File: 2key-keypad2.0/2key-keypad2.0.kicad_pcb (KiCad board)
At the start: 2 copper layers, 39.7 x 43.7 mm, 21 parts, among them SW1 SW_Push, U2 ATmega32U2-AU, Y1 16MHz

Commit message: Updated Schem
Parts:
- moved C2 9.05 mm to (141.4, 89.7), turned to 135 degrees
- moved C3 9.00 mm to (135.0, 96.1), turned to -45 degrees
- moved R4 0.47 mm to (125.9, 93.3)
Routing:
- net +5V: track 0.00 -> 90.1 mm, vias 0 -> 4
- net GND: track 6.34 -> 42.8 mm, vias 0 -> 1
- net Net-(D1-DOUT): track 0.00 -> 31.4 mm, vias 0 -> 2
- net COL0: track 0.00 -> 22.3 mm
- net D-: track 0.00 -> 22.2 mm, vias 0 -> 2
- net Net-(U2-PC1/~{RESET}): track 0.00 -> 20.0 mm, vias 0 -> 2
- net D+: track 0.00 -> 19.9 mm
- net COL1: track 0.00 -> 19.8 mm, vias 0 -> 2
- net VCC: track 0.00 -> 18.9 mm
- net XTAL1: track 0.00 -> 10.8 mm
- net LED: track 0.00 -> 7.85 mm
- net Net-(U2-UCAP): track 0.00 -> 7.63 mm
- net XTAL2: track 0.00 -> 7.24 mm
- net Net-(U2-D+): track 0.00 -> 6.96 mm
- net Net-(U2-D-): track 0.00 -> 5.49 mm
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- added copper zone on B.Cu, net GND
- added copper zone on F.Cu, net GND

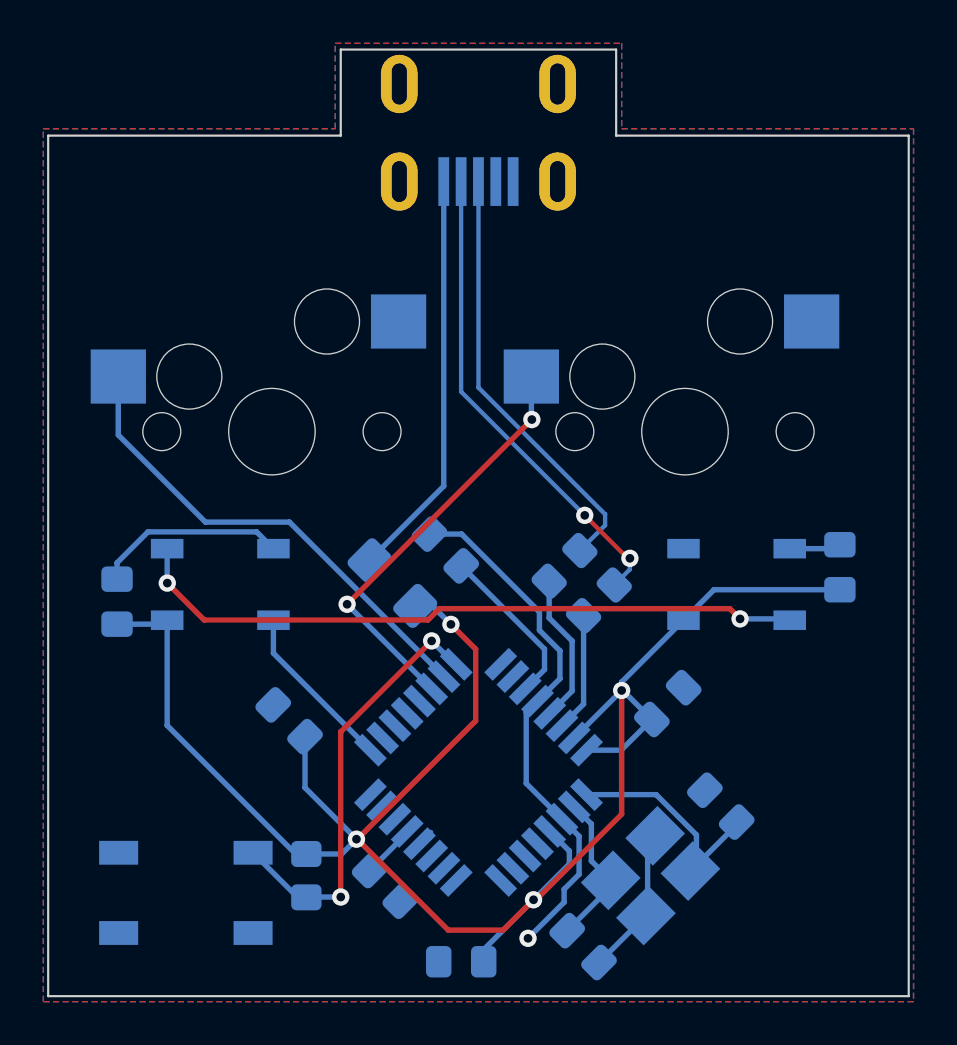
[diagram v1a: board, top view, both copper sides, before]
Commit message: Removed VIAs and equalized data traces
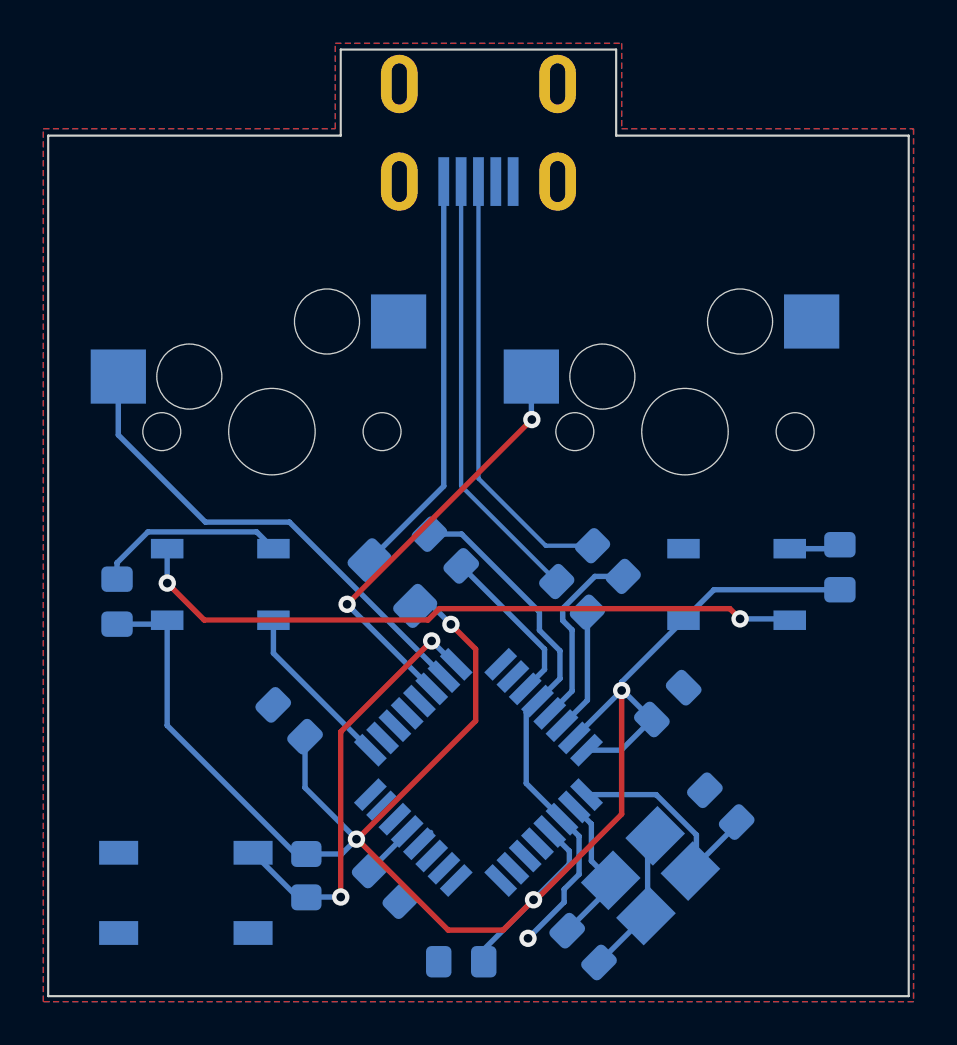
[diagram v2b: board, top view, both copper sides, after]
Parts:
- moved R1 2.01 mm to (136.1, 78.4), turned to -45 degrees
- moved R2 1.25 mm to (134.5, 80.0), turned to -45 degrees
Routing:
- net D-: track 22.2 -> 20.3 mm, vias 2 -> 0
- net Net-(U2-D+): track 6.96 -> 8.85 mm
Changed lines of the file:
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@@
   )
   (footprint "Resistor_SMD:R_0805_2012Metric_Pad1.20x1.40mm_HandSolder" (layer "B.Cu")
-    (at 135.73125 80.16875 -135)
+    (at 134.493 80.01 -45)
     (descr "Resistor SMD 0805 (2012 Metric), square (rectangular) end terminal, IPC_7351 nominal with elongated pad for handsoldering. (Body size source: IPC-SM-782 page 72, https://www.pcb-3d.com/wordpress/wp-content/uploads/ipc-sm-782a_amendment_1_and_2.pdf), generated with kicad-footprint-generator")
     (tags "resistor handsolder")
@@
     (property "ki_keywords" "R resistor")
     (attr smd)
-    (fp_text reference "R2" (at -2.918583 0.538815 45) (layer "B.SilkS")
-        (effects (font (size 1 1) (thickness 0.15)) (justify mirror))
-    )
-    (fp_text value "22" (at 0 -1.65 45) (layer "B.Fab")
-        (effects (font (size 1 1) (thickness 0.15)) (justify mirror))
-    )
-    (fp_text user "${REFERENCE}" (at 0 0 45) (layer "B.Fab")
+    (fp_text reference "R2" (at -2.918583 0.538815 135) (layer "B.SilkS")
+        (effects (font (size 1 1) (thickness 0.15)) (justify mirror))
+    )
+    (fp_text value "22" (at 0 -1.65 135) (layer "B.Fab")
+        (effects (font (size 1 1) (thickness 0.15)) (justify mirror))
+    )
+    (fp_text user "${REFERENCE}" (at 0 0 135) (layer "B.Fab")
         (effects (font (size 0.5 0.5) (thickness 0.08)) (justify mirror))
     )
@@
     (fp_line (start 1 0.625) (end 1 -0.625)
       (stroke (width 0.1) (type solid)) (layer "B.Fab"))
-    (pad "1" smd roundrect (at -1 0 225) (size 1.2 1.4) (layers "B.Cu" "B.Paste" "B.Mask") (roundrect_rratio 0.2083333333)
+    (pad "1" smd roundrect (at -1 0 315) (size 1.2 1.4) (layers "B.Cu" "B.Paste" "B.Mask") (roundrect_rratio 0.2083333333)
       (net 14 "D-") (pintype "passive"))
-    (pad "2" smd roundrect (at 1 0 225) (size 1.2 1.4) (layers "B.Cu" "B.Paste" "B.Mask") (roundrect_rratio 0.2083333333)
+    (pad "2" smd roundrect (at 1 0 315) (size 1.2 1.4) (layers "B.Cu" "B.Paste" "B.Mask") (roundrect_rratio 0.2083333333)
       (net 15 "Net-(U2-D-)") (pintype "passive"))
     (model "${KICAD6_3DMODEL_DIR}/Resistor_SMD.3dshapes/R_0805_2012Metric.wrl"
@@
   )
   (footprint "Resistor_SMD:R_0805_2012Metric_Pad1.20x1.40mm_HandSolder" (layer "B.Cu")
-    (at 134.14375 78.58125 -135)
+    (at 136.144 78.359 -45)
     (descr "Resistor SMD 0805 (2012 Metric), square (rectangular) end terminal, IPC_7351 nominal with elongated pad for handsoldering. (Body size source: IPC-SM-782 page 72, https://www.pcb-3d.com/wordpress/wp-content/uploads/ipc-sm-782a_amendment_1_and_2.pdf), generated with kicad-footprint-generator")
     (tags "resistor handsolder")
@@
     (property "ki_keywords" "R resistor")
     (attr smd)
-    (fp_text reference "R1" (at -2.828781 0 45) (layer "B.SilkS")
-        (effects (font (size 1 1) (thickness 0.15)) (justify mirror))
-    )
-    (fp_text value "22" (at 0 -1.65 45) (layer "B.Fab")
-        (effects (font (size 1 1) (thickness 0.15)) (justify mirror))
-    )
-    (fp_text user "${REFERENCE}" (at 0 0 45) (layer "B.Fab")
+    (fp_text reference "R1" (at -2.828781 0 135) (layer "B.SilkS")
+        (effects (font (size 1 1) (thickness 0.15)) (justify mirror))
+    )
+    (fp_text value "22" (at 0 -1.65 135) (layer "B.Fab")
+        (effects (font (size 1 1) (thickness 0.15)) (justify mirror))
+    )
+    (fp_text user "${REFERENCE}" (at 0 0 135) (layer "B.Fab")
         (effects (font (size 0.5 0.5) (thickness 0.08)) (justify mirror))
     )
@@
     (fp_line (start 1 0.625) (end 1 -0.625)
       (stroke (width 0.1) (type solid)) (layer "B.Fab"))
-    (pad "1" smd roundrect (at -1 0 225) (size 1.2 1.4) (layers "B.Cu" "B.Paste" "B.Mask") (roundrect_rratio 0.2083333333)
+    (pad "1" smd roundrect (at -1 0 315) (size 1.2 1.4) (layers "B.Cu" "B.Paste" "B.Mask") (roundrect_rratio 0.2083333333)
       (net 12 "D+") (pintype "passive"))
-    (pad "2" smd roundrect (at 1 0 225) (size 1.2 1.4) (layers "B.Cu" "B.Paste" "B.Mask") (roundrect_rratio 0.2083333333)
+    (pad "2" smd roundrect (at 1 0 315) (size 1.2 1.4) (layers "B.Cu" "B.Paste" "B.Mask") (roundrect_rratio 0.2083333333)
       (net 13 "Net-(U2-D+)") (pintype "passive"))
     (model "${KICAD6_3DMODEL_DIR}/Resistor_SMD.3dshapes/R_0805_2012Metric.wrl"
@@
   (segment (start 132.615 69.85) (end 132.615 71.81002) (width 0.25) (layer "B.Cu") (net 11))
   (segment (start 124.117903 80.352097) (end 123.952 80.186194) (width 0.25) (layer "B.Cu") (net 11))
-  (segment (start 130.175 70.359264) (end 136.015736 76.2) (width 0.2) (layer "B.Cu") (net 12))
-  (segment (start 136.017 76.2) (end 136.017 76.708) (width 0.2) (layer "B.Cu") (net 12))
-  (segment (start 136.017 76.708) (end 134.850857 77.874143) (width 0.2) (layer "B.Cu") (net 12))
-  (segment (start 136.015736 76.2) (end 136.017 76.2) (width 0.2) (layer "B.Cu") (net 12))
-  (segment (start 130.175 60.85625) (end 130.175 70.359264) (width 0.2) (layer "B.Cu") (net 12))
-  (segment (start 134.493 82.042) (end 134.493 84.353936) (width 0.25) (layer "B.Cu") (net 13))
+  (segment (start 130.175 60.85625) (end 130.175 74.549) (width 0.2) (layer "B.Cu") (net 12))
+  (segment (start 133.277893 77.651893) (end 135.436893 77.651893) (width 0.2) (layer "B.Cu") (net 12))
+  (segment (start 130.175 74.549) (end 133.277893 77.651893) (width 0.2) (layer "B.Cu") (net 12))
+  (segment (start 134.493 81.534) (end 134.493 84.353936) (width 0.25) (layer "B.Cu") (net 13))
   (segment (start 134.493 84.353936) (end 133.463047 85.383889) (width 0.25) (layer "B.Cu") (net 13))
-  (segment (start 133.436643 79.288357) (end 133.436643 80.985643) (width 0.25) (layer "B.Cu") (net 13))
-  (segment (start 133.436643 80.985643) (end 134.493 82.042) (width 0.25) (layer "B.Cu") (net 13))
-  (segment (start 137.058492 78.232) (end 137.16 78.232) (width 0.2) (layer "F.Cu") (net 14))
-  (segment (start 135.077246 76.250754) (end 137.058492 78.232) (width 0.2) (layer "F.Cu") (net 14))
-  (via (at 137.16 78.232) (size 0.8) (drill 0.4) (layers "F.Cu" "B.Cu") (net 14))
-  (via (at 135.077246 76.250754) (size 0.8) (drill 0.4) (layers "F.Cu" "B.Cu") (net 14))
-  (segment (start 129.375 70.548508) (end 135.077246 76.250754) (width 0.2) (layer "B.Cu") (net 14))
-  (segment (start 137.16 78.74) (end 136.438357 79.461643) (width 0.2) (layer "B.Cu") (net 14))
-  (segment (start 137.16 78.232) (end 137.16 78.74) (width 0.2) (layer "B.Cu") (net 14))
-  (segment (start 129.375 60.85625) (end 129.375 70.548508) (width 0.2) (layer "B.Cu") (net 14))
-  (segment (start 135.024143 84.954163) (end 134.028732 85.949574) (width 0.25) (layer "B.Cu") (net 15))
-  (segment (start 135.024143 80.875857) (end 135.024143 84.954163) (width 0.25) (layer "B.Cu") (net 15))
+  (segment (start 134.059421 81.100421) (end 134.493 81.534) (width 0.25) (layer "B.Cu") (net 13))
+  (segment (start 136.851107 79.066107) (end 135.542959 79.066107) (width 0.25) (layer "B.Cu") (net 13))
+  (segment (start 135.542959 79.066107) (end 134.059421 80.549645) (width 0.25) (layer "B.Cu") (net 13))
+  (segment (start 134.059421 80.549645) (end 134.059421 81.100421) (width 0.25) (layer "B.Cu") (net 13))
+  (segment (start 129.375 74.892) (end 133.785893 79.302893) (width 0.2) (layer "B.Cu") (net 14))
+  (segment (start 129.375 60.85625) (end 129.375 74.892) (width 0.2) (layer "B.Cu") (net 14))
+  (segment (start 135.200107 84.778199) (end 134.028732 85.949574) (width 0.25) (layer "B.Cu") (net 15))
+  (segment (start 135.200107 80.717107) (end 135.200107 84.778199) (width 0.25) (layer "B.Cu") (net 15))
   (segment (start 128.016 82.042) (end 123.825 86.233) (width 0.25) (layer "F.Cu") (net 16))
   (segment (start 123.825 86.233) (end 123.825 93.853) (width 0.25) (layer "F.Cu") (net 16))
